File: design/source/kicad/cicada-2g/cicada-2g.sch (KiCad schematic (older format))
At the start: 52 parts, among them J2 Host, J3 USB_OTG, J4 IPX, J5 IPX, P1 SK-C793, Q1 NMOS, Q2 NMOS, Q4 NMOS, U2 USBLC6-2SC6, U3 M3406-ADJ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

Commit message: Cicada 2G v2.1 - don't swap RX-TX
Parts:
- added LOGO1: SYM_Hot_Small, cicada-footprints:okra_logo_copper_2, symbol Graphic:SYM_Hot_Small
- R10: value 220R -> 470R
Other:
- note added: "Okra logo"
- note removed: "Swapped"
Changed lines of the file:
@@
 	14600 5150 15250 5150
 Connection ~ 14600 5150
-Text Label 15250 5150 2    50   ~ 10
+Text Label 15250 6000 2    50   ~ 10
 UART_TX_3v3
 Text Notes 14600 5350 0    50   ~ 10
@@
 	14600 6000 15250 6000
 Connection ~ 14600 6000
-Text Label 15250 6000 2    50   ~ 10
+Text Label 15250 5150 2    50   ~ 10
 UART_RX_3v3
 Text Notes 14600 6200 0    50   ~ 10
@@
 Wire Wire Line
 	13400 6000 14000 6000
-Text Notes 13150 5550 0    50   ~ 10
-Swapped
-Wire Notes Line
-	13750 5150 13500 5500
-Wire Notes Line
-	13500 5500 13700 5900
 Text Label 2000 2950 0    50   ~ 10
 UART_RX_2v8
@@
 Wire Wire Line
 	5550 2950 5550 3000
-Text Label 5550 2950 0    50   ~ 10
-5v
 Wire Wire Line
 	5550 3300 5550 3400
@@
 P 5550 3500
 F 0 "R10" H 5609 3547 50  0000 L CNN
-F 1 "220R" H 5609 3454 50  0000 L CNN
+F 1 "470R" H 5609 3454 50  0000 L CNN
 F 2 "Resistor_SMD:R_0402_1005Metric" H 5550 3500 50  0001 C CNN
 F 3 "~" H 5550 3500 50  0001 C CNN
@@
 	7100 9350 6750 9350
 Connection ~ 6750 9350
+Text Label 5550 2950 2    50   ~ 10
+V_BATT
+$Comp
+L Graphic:SYM_Hot_Small LOGO1
+U 1 1 5CEA13D2
+P 13100 6950
+F 0 "LOGO1" H 13100 7090 50  0001 C CNN
+F 1 "SYM_Hot_Small" H 13100 6825 50  0001 C CNN
+F 2 "cicada-footprints:okra_logo_copper_2" H 13100 6775 50  0001 C CNN
+F 3 "~" H 13130 6750 50  0001 C CNN
+	1    13100 6950
+	1    0    0    -1
+$EndComp
+Text Notes 13250 7000 0    118  ~ 0
+Okra logo
 $EndSCHEMATC

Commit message: Grounded PWRKEY
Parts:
- added R13: 0R, Resistor_SMD:R_0402_1005Metric, symbol Device:R
- added TP1: TestPoint, TestPoint:TestPoint_Pad_D1.5mm, symbol Connector:TestPoint
- H1, H2: footprint MountingHole_3.2mm_M3_ISO14580_Pad -> MountingHole:MountingHole_3.2mm_M3_ISO14580_Pad
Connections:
- wire segments 214 -> 219
- no-connect marks 18 -> 17
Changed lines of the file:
@@
 EESchema Schematic File Version 4
 LIBS:cicada-2g-cache
-EELAYER 29 0
+EELAYER 30 0
 EELAYER END
 $Descr A3 16535 11693
@@
 F 0 "H1" H 1300 6449 50  0000 L CNN
 F 1 "MountingHole_Pad" H 1300 6356 50  0000 L CNN
-F 2 "MountingHole_3.2mm_M3_ISO14580_Pad" H 1200 6400 50  0001 C CNN
+F 2 "MountingHole:MountingHole_3.2mm_M3_ISO14580_Pad" H 1200 6400 50  0001 C CNN
 F 3 "~" H 1200 6400 50  0001 C CNN
 	1    1200 6400
@@
 F 0 "H2" H 2300 6449 50  0000 L CNN
 F 1 "MountingHole_Pad" H 2300 6356 50  0000 L CNN
-F 2 "MountingHole_3.2mm_M3_ISO14580_Pad" H 2200 6400 50  0001 C CNN
+F 2 "MountingHole:MountingHole_3.2mm_M3_ISO14580_Pad" H 2200 6400 50  0001 C CNN
 F 3 "~" H 2200 6400 50  0001 C CNN
 	1    2200 6400
@@
 	1    0    0    -1
 $EndComp
-NoConn ~ 2550 3450
 NoConn ~ 2550 3650
 NoConn ~ 2550 4050
@@
 Text Notes 13250 7000 0    118  ~ 0
 Okra logo
+$Comp
+L Device:R R13
+U 1 1 5D94B048
+P 2250 3450
+F 0 "R13" V 2043 3450 50  0000 C CNN
+F 1 "0R" V 2134 3450 50  0000 C CNN
+F 2 "Resistor_SMD:R_0402_1005Metric" V 2180 3450 50  0001 C CNN
+F 3 "~" H 2250 3450 50  0001 C CNN
+	1    2250 3450
+	0    1    1    0
+$EndComp
+Wire Wire Line
+	2550 3450 2400 3450
+$Comp
+L power:GND #PWR0102
+U 1 1 5D95CA6E
+P 2000 3600
+F 0 "#PWR0102" H 2000 3350 50  0001 C CNN
+F 1 "GND" H 2005 3427 50  0000 C CNN
+F 2 "" H 2000 3600 50  0001 C CNN
+F 3 "" H 2000 3600 50  0001 C CNN
+	1    2000 3600
+	1    0    0    -1
+$EndComp
+Wire Wire Line
+	2000 3600 2000 3450
+Wire Wire Line
+	2000 3450 2100 3450
+$Comp
+L Connector:TestPoint TP1
+U 1 1 5D96E138
+P 4950 3550
+F 0 "TP1" H 5008 3668 50  0000 L CNN
+F 1 "TestPoint" H 5008 3577 50  0000 L CNN
+F 2 "TestPoint:TestPoint_Pad_D1.5mm" H 5150 3550 50  0001 C CNN
+F 3 "~" H 5150 3550 50  0001 C CNN
+	1    4950 3550
+	1    0    0    -1
+$EndComp
+Wire Wire Line
+	4950 3550 4950 3750
+Wire Wire Line
+	4950 3750 4150 3750
 $EndSCHEMATC

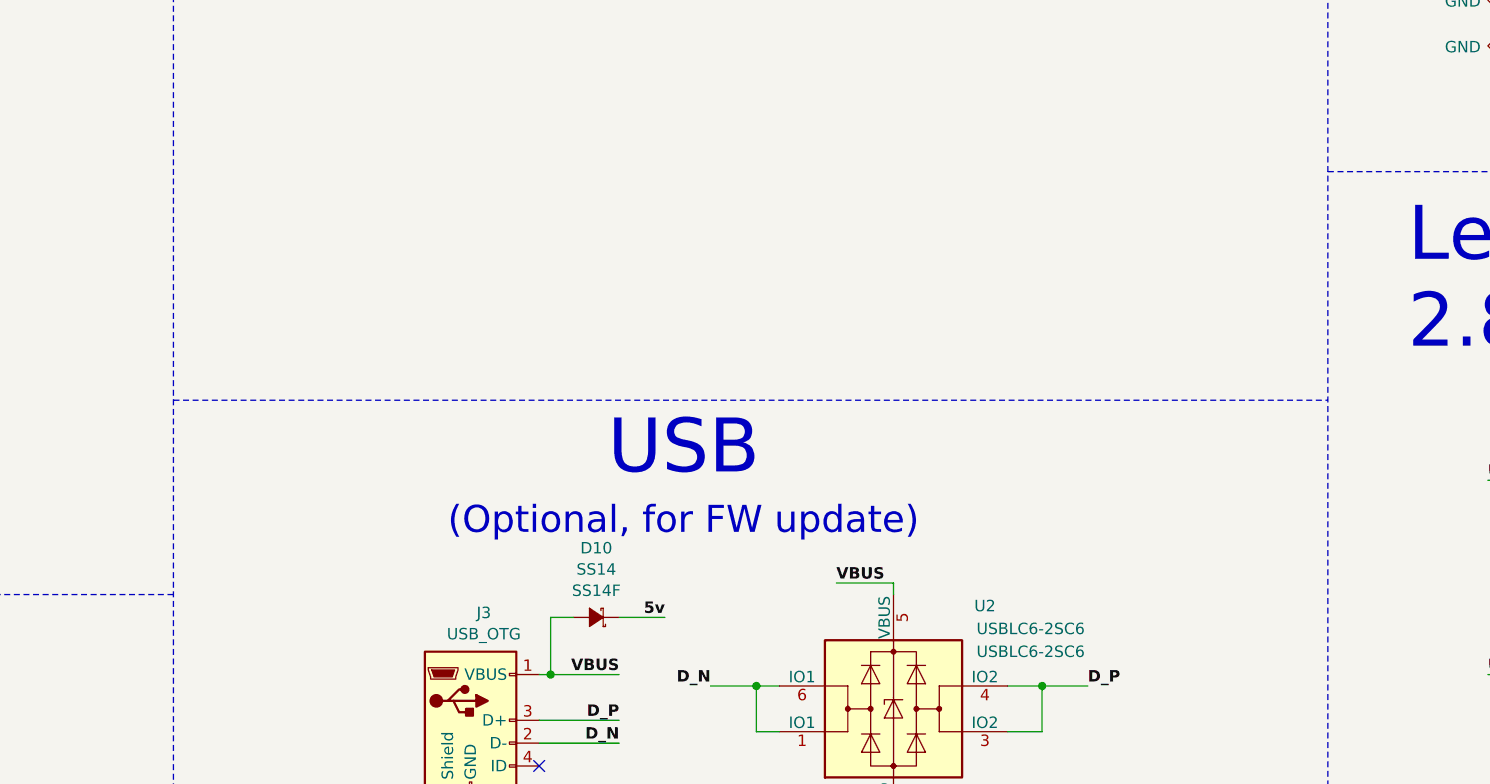
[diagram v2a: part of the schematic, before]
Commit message: Added POWER pull-up when powered from USB
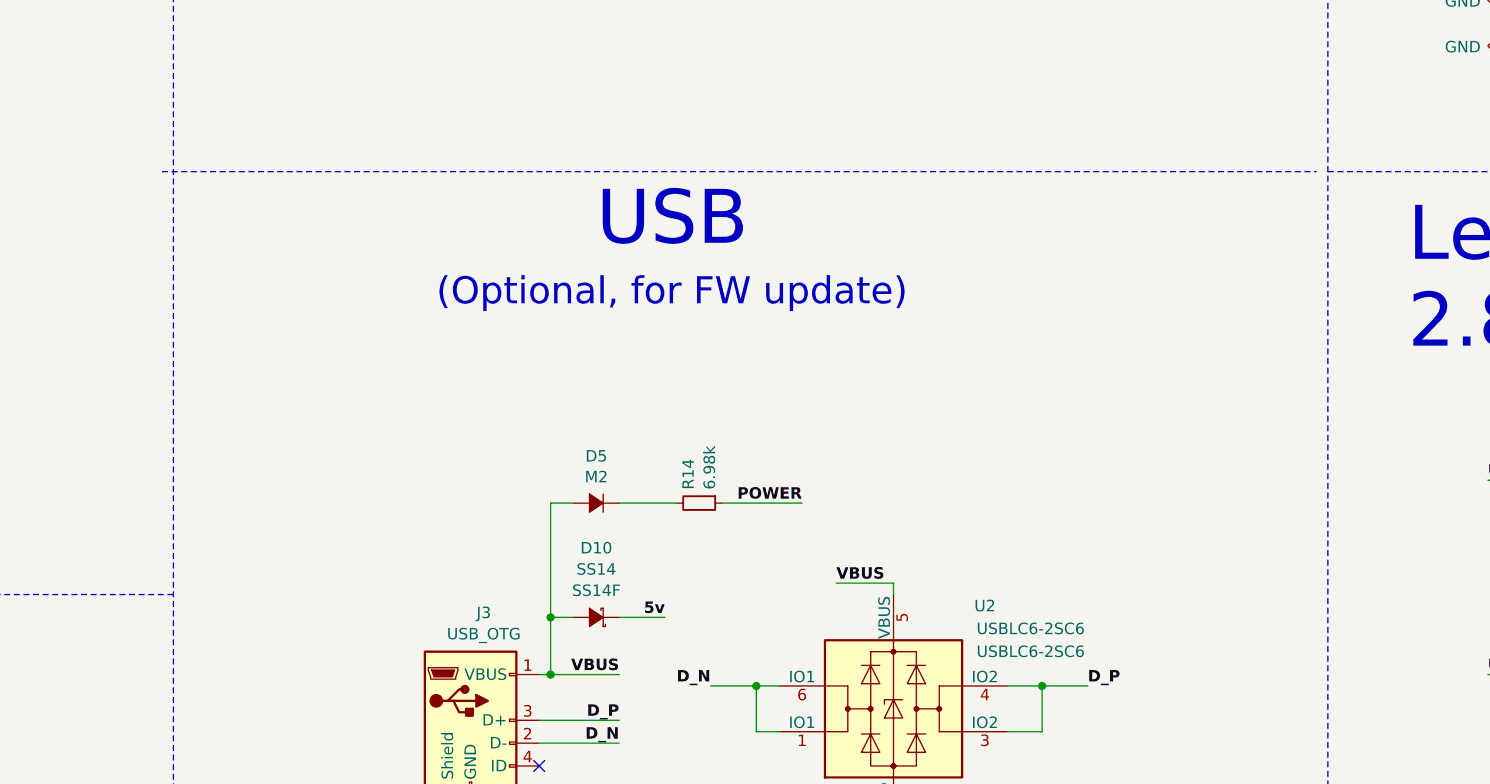
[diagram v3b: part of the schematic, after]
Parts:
- added D5: M2, Diode_SMD:D_SMA, symbol Device:D_Small_ALT
- added R14: 6.98k, Resistor_SMD:R_0402_1005Metric, symbol Device:R_Small
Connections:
- wire segments 219 -> 223
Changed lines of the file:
@@
 Power supply
-Wire Notes Line width 24
-	12700 3800 16050 3800
 Wire Notes Line width 24
 	12700 500  12700 9950
@@
 Text Notes 9050 850  0    236  ~ 0
 Antennas
-Wire Notes Line width 24
-	7650 4800 12700 4800
 Text Notes 2600 1650 0    236  ~ 0
 SIM800C
@@
 Text Label 9800 5750 2    50   ~ 10
 5v
-Text Notes 8850 5400 0    118  ~ 0
-(Optional, for FW update)
-Text Notes 9550 5150 0    236  ~ 0
-USB
 Text Notes 13050 4600 0    236  ~ 0
 Level shifters\n2.8v <-> 3.3v
@@
 Wire Wire Line
 	4950 3750 4150 3750
+Wire Notes Line width 24
+	12700 3800 16050 3800
+Wire Notes Line width 24
+	7600 3800 12650 3800
+Text Notes 8800 4400 0    118  ~ 0
+(Optional, for FW update)
+Text Notes 9500 4150 0    236  ~ 0
+USB
+$Comp
+L Device:D_Small_ALT D5
+U 1 1 5DA09083
+P 9500 5250
+F 0 "D5" H 9500 5045 50  0000 C CNN
+F 1 "M2" H 9500 5136 50  0000 C CNN
+F 2 "Diode_SMD:D_SMA" V 9500 5250 50  0001 C CNN
+F 3 "~" V 9500 5250 50  0001 C CNN
+	1    9500 5250
+	-1   0    0    1
+$EndComp
+Wire Wire Line
+	9300 5750 9300 5250
+Wire Wire Line
+	9300 5250 9400 5250
+Connection ~ 9300 5750
+$Comp
+L Device:R_Small R?
+U 1 1 5DA1AAA4
+P 9950 5250
+AR Path="/5C2BA648/5DA1AAA4" Ref="R?"  Part="1"
+AR Path="/5C38341E/5DA1AAA4" Ref="R?"  Part="1"
+AR Path="/5C150E9A/5DA1AAA4" Ref="R?"  Part="1"
+AR Path="/5DA1AAA4" Ref="R14"  Part="1"
+F 0 "R14" H 9891 5203 50  0000 R CNN
+F 1 "6.98k" H 9891 5296 50  0000 R CNN
+F 2 "Resistor_SMD:R_0402_1005Metric" H 9950 5250 50  0001 C CNN
+F 3 "~" H 9950 5250 50  0001 C CNN
+F 4 "0.0015" H 4050 -2450 50  0001 C CNN "SRC_USD_Q1000"
+	1    9950 5250
+	0    1    1    0
+$EndComp
+Wire Wire Line
+	9850 5250 9600 5250
+Text Label 10400 5250 2    50   ~ 10
+POWER
+Wire Wire Line
+	10400 5250 10050 5250
 $EndSCHEMATC

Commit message: Replaced FET level shifters with 74LVC1G17GW
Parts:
- removed Q2, Q4: NMOS, Package_TO_SOT_SMD:SOT-23, symbol Device:Q_NMOS_GSD
- removed R5, R6: 4.7k, Resistor_SMD:R_0402_1005Metric, symbol Device:R_Small
- added C7, C8: DNP, Capacitor_SMD:C_0402_1005Metric, symbol Device:C
- added U1, U5: 74LVC1G17GW, Package_TO_SOT_SMD:SOT-353_SC-70-5, symbol 74xGxx:74LVC1G17
- R3, R4: value 4.7k -> 470R
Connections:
- wire segments 223 -> 216
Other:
- note removed: "Vth < 1.8v"

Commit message: Fixed version and changed LED driver
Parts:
- removed Q1: NMOS, Package_TO_SOT_SMD:SOT-23, symbol Device:Q_NMOS_GSD
- removed R11: 40.2k, Resistor_SMD:R_0402_1005Metric, symbol Device:R_Small
- added Q?: BC847C, Package_TO_SOT_SMD:SOT-23, symbol Transistor_BJT:BC847
- R1: value DNP -> 150k; DNP DNP -> (none)
- R10, R3, R4: value 470R -> 330R
- R2: value 340k -> 150k
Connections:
- wire segments 216 -> 210
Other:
- note added: "VER_2 = 2"
- note removed: "VER_2 = 1"
- moved on the sheet: D4, R10
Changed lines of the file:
@@
 EESchema Schematic File Version 4
-LIBS:cicada-2g-cache
 EELAYER 30 0
 EELAYER END
@@
 P 14950 2950
 F 0 "R1" V 14659 2950 50  0000 C CNN
-F 1 "DNP" V 14752 2950 50  0000 C CNN
+F 1 "150k" V 14752 2950 50  0000 C CNN
 F 2 "Resistor_SMD:R_0402_1005Metric" H 14950 2950 50  0001 C CNN
 F 3 "~" H 14950 2950 50  0001 C CNN
-F 4 "DNP" V 14845 2950 50  0000 C CNN "DNP"
+F 4 "" V 14845 2950 50  0000 C CNN "DNP"
 F 5 "0" H 150 300 50  0001 C CNN "SRC_USD_Q1000"
 	1    14950 2950
@@
 P 15200 3050
 F 0 "R2" V 14800 3050 50  0000 C CNN
-F 1 "340k" V 14900 3050 50  0000 C CNN
+F 1 "150k" V 14900 3050 50  0000 C CNN
 F 2 "Resistor_SMD:R_0402_1005Metric" H 15200 3050 50  0001 C CNN
 F 3 "~" H 15200 3050 50  0001 C CNN
@@
 VER_1 = 2
 Text Notes 15300 2700 0    50   ~ 10
-VER_2 = 1
+VER_2 = 2
 Text Label 4550 2750 2    50   ~ 10
 SIM_VCC
@@
 	4150 2750 4550 2750
 Wire Wire Line
-	5550 2950 5550 3000
-Wire Wire Line
-	5550 3300 5550 3400
+	5550 3150 5550 3200
 $Comp
 L Device:LED_ALT D4
 U 1 1 5CA724C2
-P 5550 3150
-F 0 "D4" V 5590 3029 50  0000 R CNN
-F 1 "LED_B" V 5497 3029 50  0000 R CNN
-F 2 "Diode_SMD:D_0603_1608Metric" H 5550 3150 50  0001 C CNN
-F 3 "~" H 5550 3150 50  0001 C CNN
-F 4 "ORH-B36G" H -650 1850 50  0001 C CNN "MPN"
-F 5 "Orient" H -650 1850 50  0001 C CNN "Manufacturer"
-F 6 "lcsc" H -650 1850 50  0001 C CNN "SOURCE"
-F 7 "C193191" H -650 1850 50  0001 C CNN "SRCPN"
-F 8 "0.0048" H -650 1850 50  0001 C CNN "SRC_USD_Q1000"
-	1    5550 3150
+P 5550 3350
+F 0 "D4" V 5590 3229 50  0000 R CNN
+F 1 "LED_B" V 5497 3229 50  0000 R CNN
+F 2 "Diode_SMD:D_0603_1608Metric" H 5550 3350 50  0001 C CNN
+F 3 "~" H 5550 3350 50  0001 C CNN
+F 4 "ORH-B36G" H -650 2050 50  0001 C CNN "MPN"
+F 5 "Orient" H -650 2050 50  0001 C CNN "Manufacturer"
+F 6 "lcsc" H -650 2050 50  0001 C CNN "SOURCE"
+F 7 "C193191" H -650 2050 50  0001 C CNN "SRCPN"
+F 8 "0.0048" H -650 2050 50  0001 C CNN "SRC_USD_Q1000"
+	1    5550 3350
 	0    -1   -1   0
 $EndComp
-Wire Wire Line
-	5550 3600 5550 3650
 $Comp
 L Device:R_Small R10
 U 1 1 5CA6DA64
-P 5550 3500
-F 0 "R10" H 5609 3547 50  0000 L CNN
-F 1 "470R" H 5609 3454 50  0000 L CNN
-F 2 "Resistor_SMD:R_0402_1005Metric" H 5550 3500 50  0001 C CNN
-F 3 "~" H 5550 3500 50  0001 C CNN
-F 4 "0.0015" H -650 1850 50  0001 C CNN "SRC_USD_Q1000"
-	1    5550 3500
-	1    0    0    -1
-$EndComp
-Wire Wire Line
-	5550 4150 5550 4250
-Connection ~ 5550 4150
-Wire Wire Line
-	5200 4150 5550 4150
-Wire Wire Line
-	5200 4100 5200 4150
-Wire Wire Line
-	5550 4050 5550 4150
-Wire Wire Line
-	5200 3850 5250 3850
-Wire Wire Line
-	5200 3900 5200 3850
-$Comp
-L Device:R_Small R11
-U 1 1 5CA59C49
-P 5200 4000
-F 0 "R11" H 5450 4050 50  0000 R CNN
-F 1 "40.2k" H 5450 3950 50  0000 R CNN
-F 2 "Resistor_SMD:R_0402_1005Metric" H 5200 4000 50  0001 C CNN
-F 3 "~" H 5200 4000 50  0001 C CNN
-F 4 "0.0015" H -650 1850 50  0001 C CNN "SRC_USD_Q1000"
-	1    5200 4000
-	-1   0    0    -1
-$EndComp
-$Comp
-L Device:Q_NMOS_GSD Q1
-U 1 1 5CA4A376
-P 5450 3850
-F 0 "Q1" V 5700 3550 50  0000 C CNN
-F 1 "NMOS" V 5700 3900 50  0000 C CNN
-F 2 "Package_TO_SOT_SMD:SOT-23" H 5650 3950 50  0001 C CNN
-F 3 "~" H 5450 3850 50  0001 C CNN
-F 4 "WST3400S" V 5800 3750 50  0000 C CNN "MPN"
-F 5 "AO3400 analog" H -650 1850 50  0001 C CNN "Description"
-F 6 "Winsok Semicon" H -650 1850 50  0001 C CNN "Manufacturer"
-F 7 "lcsc" H -650 1850 50  0001 C CNN "SOURCE"
-F 8 "C105164" H -650 1850 50  0001 C CNN "SRCPN"
-F 9 "0.0306" H -650 1850 50  0001 C CNN "SRC_USD_Q1000"
-	1    5450 3850
+P 5550 4150
+F 0 "R10" H 5609 4197 50  0000 L CNN
+F 1 "330R" H 5609 4104 50  0000 L CNN
+F 2 "Resistor_SMD:R_0402_1005Metric" H 5550 4150 50  0001 C CNN
+F 3 "~" H 5550 4150 50  0001 C CNN
+F 4 "0.0015" H -650 2500 50  0001 C CNN "SRC_USD_Q1000"
+	1    5550 4150
 	1    0    0    -1
 $EndComp
@@
 L power:GND #PWR08
 U 1 1 5CA61B67
-P 5550 4250
-F 0 "#PWR08" H 5550 4000 50  0001 C CNN
-F 1 "GND" H 5555 4073 50  0000 C CNN
-F 2 "" H 5550 4250 50  0001 C CNN
-F 3 "" H 5550 4250 50  0001 C CNN
-	1    5550 4250
+P 5550 4450
+F 0 "#PWR08" H 5550 4200 50  0001 C CNN
+F 1 "GND" H 5555 4273 50  0000 C CNN
+F 2 "" H 5550 4450 50  0001 C CNN
+F 3 "" H 5550 4450 50  0001 C CNN
+	1    5550 4450
 	1    0    0    -1
 $EndComp
@@
 	10150 1150 10700 1150
 Wire Wire Line
-	4150 3850 5200 3850
-Connection ~ 5200 3850
-Wire Wire Line
 	5750 9700 6000 9700
 Connection ~ 5750 9700
@@
 	7100 9350 6750 9350
 Connection ~ 6750 9350
-Text Label 5550 2950 2    50   ~ 10
+Text Label 5550 3150 2    50   ~ 10
 V_BATT
 $Comp
@@
 P 14500 6650
 F 0 "R4" V 14301 6650 50  0000 C CNN
-F 1 "470R" V 14394 6650 50  0000 C CNN
+F 1 "330R" V 14394 6650 50  0000 C CNN
 F 2 "Resistor_SMD:R_0402_1005Metric" H 14500 6650 50  0001 C CNN
 F 3 "~" H 14500 6650 50  0001 C CNN
@@
 P 14300 5150
 F 0 "R3" V 14101 5150 50  0000 C CNN
-F 1 "470R" V 14194 5150 50  0000 C CNN
+F 1 "330R" V 14194 5150 50  0000 C CNN
 F 2 "Resistor_SMD:R_0402_1005Metric" H 14300 5150 50  0001 C CNN
 F 3 "~" H 14300 5150 50  0001 C CNN
@@
 	13150 5150 14000 5150
 Connection ~ 14000 5150
+Wire Wire Line
+	5550 4250 5550 4450
+Wire Wire Line
+	4150 3850 5250 3850
+$Comp
+L Transistor_BJT:BC847 Q?
+U 1 1 5D9812C8
+P 5450 3850
+F 0 "Q?" H 5641 3896 50  0000 L CNN
+F 1 "BC847C" H 5641 3805 50  0000 L CNN
+F 2 "Package_TO_SOT_SMD:SOT-23" H 5650 3775 50  0001 L CIN
+F 3 "http://www.infineon.com/dgdl/Infineon-BC847SERIES_BC848SERIES_BC849SERIES_BC850SERIES-DS-v01_01-en.pdf?fileId=db3a304314dca389011541d4630a1657" H 5450 3850 50  0001 L CNN
+F 4 "Guangdong Hottech" H 5450 3850 50  0001 C CNN "Manufacturer"
+F 5 "BC847C" H 5450 3850 50  0001 C CNN "MPN"
+F 6 "lcsc" H 5450 3850 50  0001 C CNN "SOURCE"
+F 7 "C181141" H 5450 3850 50  0001 C CNN "SRCPN"
+F 8 "0.0043" H 5450 3850 50  0001 C CNN "SRC_USD_Q1000"
+	1    5450 3850
+	1    0    0    -1
+$EndComp
+Wire Wire Line
+	5550 3500 5550 3650
 $EndSCHEMATC

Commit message: Updated connector and capacitors
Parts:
- removed C15, C23: 330uF 6.3v, Capacitor_THT:CP_Radial_D6.3mm_P2.50mm, symbol Device:CP_Small
- added C10, C11, C12: 1000uF 10v, Capacitor_THT:CP_Radial_D8.0mm_P3.50mm, symbol Device:CP_Small
- added TP2, TP3, TP4: TestPoint, TestPoint:TestPoint_Pad_D1.5mm, symbol Connector:TestPoint
- C14, C5: value 330uF 6.3v -> 1000uF 10v; footprint Capacitor_THT:CP_Radial_D6.3mm_P2.50mm -> Capacitor_THT:CP_Radial_D8.0mm_P3.50mm; SRCPN C43322 -> C3299; SRC_USD_Q1000 0.0103 -> 0.0171
- J2: footprint Connector_PinSocket_2.54mm:PinSocket_2x08_P2.54mm_Vertical -> Connector_PinSocket_2.54mm:PinSocket_2x10_P2.54mm_Vertical; symbol Connector_Generic:Conn_02x08_Odd_Even -> Connector_Generic:Conn_02x10_Odd_Even; Description Generic 2x8 2.54mm Shrouded Male -> Generic 2x10 2.54mm Female; SRCPN C30734 -> C30867; SRC_USD_Q1000 0.0586 -> 0.0695
- gave numbers to parts that had none: 1
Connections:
- wire segments 210 -> 224
- no-connect marks 17 -> 21
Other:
- moved on the sheet: C14, C16, C17, C18, C19, C20, C21, C22, L4, R1, R19, R2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

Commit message: Updated PCB
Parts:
- removed U1, U5: 74LVC1G17GW, Package_TO_SOT_SMD:SOT-353_SC-70-5, symbol 74xGxx:74LVC1G17
- added U1, U5: 74LVC1G17, Package_TO_SOT_SMD:SOT-353_SC-70-5, symbol 74lvc1g17:74LVC1G17
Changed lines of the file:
@@
 	10400 5250 10050 5250
-$Comp
-L 74xGxx:74LVC1G17 U1
-U 1 1 5DA67831
-P 14050 6650
-F 0 "U1" H 14025 6917 50  0000 C CNN
-F 1 "74LVC1G17GW" H 14025 6826 50  0000 C CNN
-F 2 "Package_TO_SOT_SMD:SOT-353_SC-70-5" H 14050 6650 50  0001 C CNN
-F 3 "http://www.ti.com/lit/sg/scyt129e/scyt129e.pdf" H 14050 6650 50  0001 C CNN
-	1    14050 6650
-	1    0    0    -1
-$EndComp
 $Comp
 L Device:R_Small R?
@@
 Wire Wire Line
 	14050 6850 14050 6750
-$Comp
-L 74xGxx:74LVC1G17 U5
-U 1 1 5DB1EA85
-P 14700 5150
-F 0 "U5" H 14675 5417 50  0000 C CNN
-F 1 "74LVC1G17GW" H 14675 5326 50  0000 C CNN
-F 2 "Package_TO_SOT_SMD:SOT-353_SC-70-5" H 14700 5150 50  0001 C CNN
-F 3 "http://www.ti.com/lit/sg/scyt129e/scyt129e.pdf" H 14700 5150 50  0001 C CNN
-	1    14700 5150
-	-1   0    0    -1
-$EndComp
 $Comp
 L power:GND #PWR0105
@@
 Wire Wire Line
 	1050 9050 1100 9050
+$Comp
+L 74lvc1g17:74LVC1G17 U1
+U 1 1 5DB3688C
+P 14050 6650
+F 0 "U1" H 14344 6696 50  0000 L CNN
+F 1 "74LVC1G17" H 14344 6605 50  0000 L CNN
+F 2 "Package_TO_SOT_SMD:SOT-353_SC-70-5" H 14050 6650 50  0001 C CNN
+F 3 "http://www.ti.com/lit/sg/scyt129e/scyt129e.pdf" H 14050 6650 50  0001 C CNN
+	1    14050 6650
+	1    0    0    -1
+$EndComp
+$Comp
+L 74lvc1g17:74LVC1G17 U5
+U 1 1 5DB36CB4
+P 14700 5150
+F 0 "U5" H 14356 5196 50  0000 R CNN
+F 1 "74LVC1G17" H 14356 5105 50  0000 R CNN
+F 2 "Package_TO_SOT_SMD:SOT-353_SC-70-5" H 14700 5150 50  0001 C CNN
+F 3 "http://www.ti.com/lit/sg/scyt129e/scyt129e.pdf" H 14700 5150 50  0001 C CNN
+	1    14700 5150
+	-1   0    0    -1
+$EndComp
 $EndSCHEMATC

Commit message: Generated manufacturing package
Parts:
- C10: value 1000uF 10v -> DNP 1000uF 10v
- C16: MPN CL10A105KO8NNNC -> 0402CG330J500NT; Manufacturer Samsung -> Guangdong Fenghua Advanced Tech; SRCPN C59782 -> C1562; SRC_USD_Q1000 0.0050 -> 0.0015
- C17: MPN 0603B104K500NT -> 0402CG101J500NT; SRCPN C30926 -> C1546; SRC_USD_Q1000 0.0036 -> 0.0015
- C6, C9: SRC_USD_Q1000 0.0015 -> (none)
- C7, C8: DNP (none) -> DNP
- D5: value M2 -> SS14; MPN (none) -> SS14F; Manufacturer (none) -> MDD; SOURCE (none) -> lcsc; SRCPN (none) -> C64880; SRC_USD_Q1000 (none) -> 0.0080
- J5: value IPX -> DNP IPX; DNP (none) -> DNP
- Q1: value BC847C -> 2N7002; symbol Transistor_BJT:BC847 -> Transistor_FET:2N7002; MPN BC847C -> 2N7002; SRCPN C181141 -> C181082; SRC_USD_Q1000 0.0043 -> 0.0074
- R1, R2: MPN (none) -> RC0402JR-07150KL; Manufacturer (none) -> YAGEO; SOURCE (none) -> lcsc; SRCPN (none) -> C137919; SRC_USD_Q1000 0 -> 0.0013
- R10: value 330R -> 1K; MPN (none) -> RC0402JR-071KL; Manufacturer (none) -> YAGEO; SOURCE (none) -> lcsc; SRCPN (none) -> C105637; SRC_USD_Q1000 0.0015 -> 0.0003
- R12: MPN (none) -> RC0402FR-070RL; Manufacturer (none) -> YAGEO; SOURCE (none) -> lcsc; SRCPN (none) -> C106231; SRC_USD_Q1000 0.0015 -> 0.0004
- R13: MPN (none) -> RC0402FR-070RL; Manufacturer (none) -> YAGEO; SOURCE (none) -> lcsc; SRCPN (none) -> C106231; SRC_USD_Q1000 (none) -> 0.0004
- R14, R23: MPN (none) -> RC0402FR-076K98L; Manufacturer (none) -> YAGEO; SOURCE (none) -> lcsc; SRCPN (none) -> C137944; SRC_USD_Q1000 0.0015 -> 0.0019
- R19, R22: MPN (none) -> RC0402FR-0740K2L; Manufacturer (none) -> YAGEO; SOURCE (none) -> lcsc; SRCPN (none) -> C137983; SRC_USD_Q1000 0.0015 -> 0.0004
- R3, R4: MPN (none) -> RC0402FR-07330RL; Manufacturer (none) -> YAGEO; SOURCE (none) -> lcsc; SRCPN (none) -> C105875; SRC_USD_Q1000 0.0015 -> 0.0004
- R7, R8, R9: MPN (none) -> RC0402FR-0722RL; Manufacturer (none) -> YAGEO; SOURCE (none) -> lcsc; SRCPN (none) -> C114765; SRC_USD_Q1000 0.0015 -> 0.0004
- U1, U5: MPN (none) -> 74LVC1G17GW; Manufacturer (none) -> NXP Semicon; SOURCE (none) -> lcsc; SRCPN (none) -> C124293; SRC_USD_Q1000 (none) -> 0.0185
- U4: MPN (none) -> SIM800C; Manufacturer (none) -> Simcom; SOURCE (none) -> Tobao; SRCPN (none) -> https://item.taobao.com/item.htm?id=45289949668; SRC_USD_Q1000 (none) -> 2.24
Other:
- moved on the sheet: D4, R10
